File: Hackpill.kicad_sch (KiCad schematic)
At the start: 23 parts, among them J1 Conn_01x04, J2 USB_C_Receptacle_USB2.0_16P, J3 Conn_01x22, J4 Conn_01x22, SW1 SW_Push, U1 STM32F042C6Tx, U2 AMS1117-3.3, U3 USBLC6-2SC6

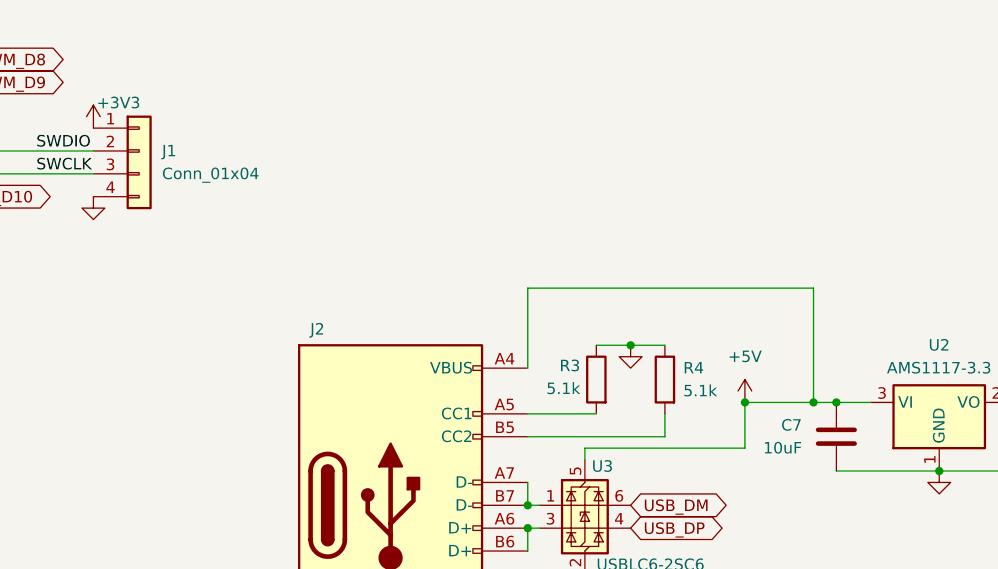
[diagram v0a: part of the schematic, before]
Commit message: Add diode to USB, rename files, add prod files
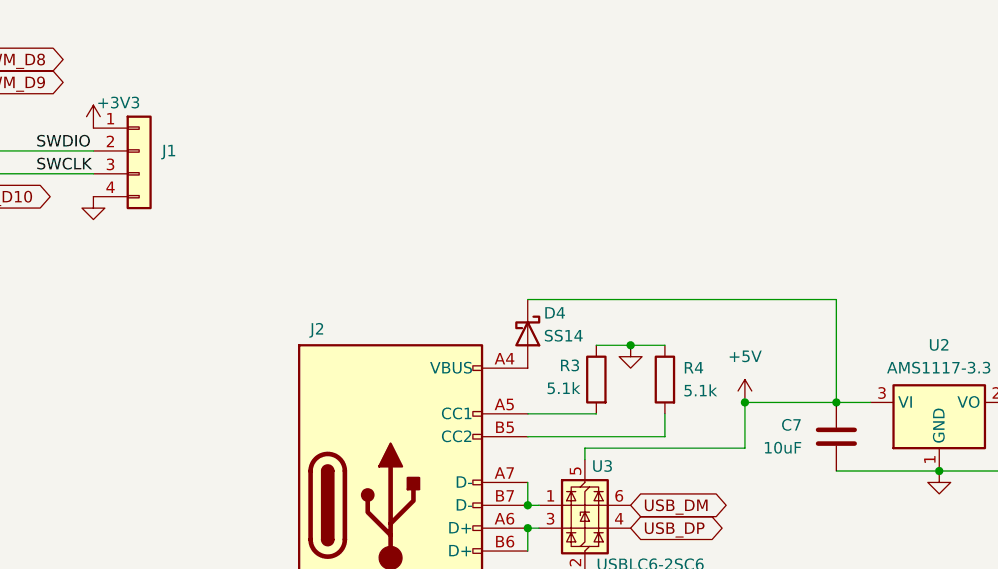
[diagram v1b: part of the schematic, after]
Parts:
- added D4: SS14, Diode_SMD:D_SMA, symbol Diode:SS14
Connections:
- net +5V: now also D4.1 (K); no longer J2.A4 (VBUS), J2.A9 (VBUS), J2.B4 (VBUS), J2.B9 (VBUS)
- new net: D4.2 (A), J2.A4 (VBUS), J2.A9 (VBUS), J2.B4 (VBUS), J2.B9 (VBUS)
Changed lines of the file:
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@@
 	)
 	(junction
-		(at 226.06 104.14)
-		(diameter 0)
-		(color 0 0 0 0)
-	)
-	(junction
 		(at 251.46 104.14)
 		(diameter 0)
@@
 	(wire
 		(pts
-			(xy 226.06 104.14) (xy 228.6 104.14)
+			(xy 171.45 138.43) (xy 179.07 138.43)
 		)
 		(stroke
@@
 	(wire
 		(pts
-			(xy 171.45 138.43) (xy 179.07 138.43)
+			(xy 101.6 29.21) (xy 93.98 29.21)
 		)
 		(stroke
@@
 	(wire
 		(pts
-			(xy 101.6 29.21) (xy 93.98 29.21)
+			(xy 218.44 109.22) (xy 218.44 104.14)
 		)
 		(stroke
@@
 	(wire
 		(pts
-			(xy 218.44 109.22) (xy 218.44 104.14)
+			(xy 121.92 76.2) (xy 146.05 76.2)
 		)
 		(stroke
@@
 	(wire
 		(pts
-			(xy 121.92 76.2) (xy 146.05 76.2)
+			(xy 64.77 43.18) (xy 64.77 44.45)
 		)
 		(stroke
@@
 	(wire
 		(pts
-			(xy 64.77 43.18) (xy 64.77 44.45)
+			(xy 194.31 92.71) (xy 228.6 92.71)
 		)
 		(stroke
@@
 	(wire
 		(pts
-			(xy 218.44 104.14) (xy 226.06 104.14)
+			(xy 218.44 104.14) (xy 228.6 104.14)
 		)
 		(stroke
@@
 	(wire
 		(pts
-			(xy 194.31 100.33) (xy 194.31 91.44)
-		)
-		(stroke
-			(width 0)
-			(type default)
-		)
-	)
-	(wire
-		(pts
 			(xy 71.12 29.21) (xy 59.69 29.21)
 		)
@@
 	(wire
 		(pts
-			(xy 194.31 91.44) (xy 226.06 91.44)
-		)
-		(stroke
-			(width 0)
-			(type default)
-		)
-	)
-	(wire
-		(pts
 			(xy 93.98 29.21) (xy 82.55 29.21)
 		)
@@
 	(wire
 		(pts
-			(xy 226.06 91.44) (xy 226.06 104.14)
+			(xy 228.6 92.71) (xy 228.6 104.14)
 		)
 		(stroke
@@
 		)
 		(instances
-			(project "Workshop_PCB"
+			(project "Hackpill"
 				(path "/c0781056-ba6f-4324-98d3-3fa2d5c57644"
 					(reference "#PWR022")
@@
 		)
 		(instances
-			(project "Workshop_PCB"
+			(project "Hackpill"
 				(path "/c0781056-ba6f-4324-98d3-3fa2d5c57644"
 					(reference "C3")
@@
 		)
 		(instances
-			(project "Workshop_PCB"
+			(project "Hackpill"
 				(path "/c0781056-ba6f-4324-98d3-3fa2d5c57644"
 					(reference "#PWR013")
@@
 		)
 		(instances
-			(project "Workshop_PCB"
+			(project "Hackpill"
 				(path "/c0781056-ba6f-4324-98d3-3fa2d5c57644"
 					(reference "U1")
@@
 		)
 		(instances
-			(project "Workshop_PCB"
+			(project "Hackpill"
 				(path "/c0781056-ba6f-4324-98d3-3fa2d5c57644"
 					(reference "#PWR05")
@@
 		)
 		(instances
-			(project "Workshop_PCB"
+			(project "Hackpill"
 				(path "/c0781056-ba6f-4324-98d3-3fa2d5c57644"
 					(reference "C7")
@@
 		)
 		(instances
-			(project "Workshop_PCB"
+			(project "Hackpill"
 				(path "/c0781056-ba6f-4324-98d3-3fa2d5c57644"
 					(reference "U2")
@@
 		)
 		(instances
-			(project "Workshop_PCB"
+			(project "Hackpill"
 				(path "/c0781056-ba6f-4324-98d3-3fa2d5c57644"
 					(reference "D2")
@@
 		)
 		(instances
-			(project "Workshop_PCB"
+			(project "Hackpill"
 				(path "/c0781056-ba6f-4324-98d3-3fa2d5c57644"
 					(reference "D1")
@@
 		)
 		(instances
-			(project "Workshop_PCB"
+			(project "Hackpill"
 				(path "/c0781056-ba6f-4324-98d3-3fa2d5c57644"
 					(reference "#PWR014")
@@
 		)
 		(instances
-			(project "Workshop_PCB"
+			(project "Hackpill"
 				(path "/c0781056-ba6f-4324-98d3-3fa2d5c57644"
 					(reference "#PWR03")
@@
 		)
 		(instances
-			(project "Workshop_PCB"
+			(project "Hackpill"
 				(path "/c0781056-ba6f-4324-98d3-3fa2d5c57644"
 					(reference "#PWR024")
@@
 		)
 		(instances
-			(project "Workshop_PCB"
+			(project "Hackpill"
 				(path "/c0781056-ba6f-4324-98d3-3fa2d5c57644"
 					(reference "C8")
@@
 		)
 		(instances
-			(project "Workshop_PCB"
+			(project "Hackpill"
 				(path "/c0781056-ba6f-4324-98d3-3fa2d5c57644"
 					(reference "#PWR015")
@@
 		)
 		(instances
-			(project "Workshop_PCB"
+			(project "Hackpill"
 				(path "/c0781056-ba6f-4324-98d3-3fa2d5c57644"
 					(reference "R4")
@@
 		)
 		(instances
-			(project "Workshop_PCB"
+			(project "Hackpill"
 				(path "/c0781056-ba6f-4324-98d3-3fa2d5c57644"
 					(reference "C6")
@@
 		)
 		(instances
-			(project "Workshop_PCB"
+			(project "Hackpill"
 				(path "/c0781056-ba6f-4324-98d3-3fa2d5c57644"
 					(reference "C5")
@@
 		)
 		(instances
-			(project "Workshop_PCB"
+			(project "Hackpill"
 				(path "/c0781056-ba6f-4324-98d3-3fa2d5c57644"
 					(reference "J2")
@@
 		)
 		(instances
-			(project "Workshop_PCB"
+			(project "Hackpill"
 				(path "/c0781056-ba6f-4324-98d3-3fa2d5c57644"
 					(reference "SW1")
@@
 		)
 		(instances
-			(project "Workshop_PCB"
+			(project "Hackpill"
 				(path "/c0781056-ba6f-4324-98d3-3fa2d5c57644"
 					(reference "#PWR021")
@@
 		)
 		(instances
-			(project "Workshop_PCB"
+			(project "Hackpill"
 				(path "/c0781056-ba6f-4324-98d3-3fa2d5c57644"
 					(reference "#PWR020")
@@
 		)
 		(instances
-			(project "Workshop_PCB"
+			(project "Hackpill"
 				(path "/c0781056-ba6f-4324-98d3-3fa2d5c57644"
 					(reference "#PWR06")
@@
 				)
 				(justify left)
+				(hide yes)
 			)
 		)
@@
 		)
 		(instances
-			(project "Workshop_PCB"
+			(project "Hackpill"
 				(path "/c0781056-ba6f-4324-98d3-3fa2d5c57644"
 					(reference "J1")
@@
 		)
 		(instances
-			(project "Workshop_PCB"
+			(project "Hackpill"
 				(path "/c0781056-ba6f-4324-98d3-3fa2d5c57644"
 					(reference "U3")
@@
 		)
 		(instances
-			(project "Workshop_PCB"
+			(project "Hackpill"
 				(path "/c0781056-ba6f-4324-98d3-3fa2d5c57644"
 					(reference "#PWR08")
@@
 		)
 		(instances
-			(project "Workshop_PCB"
+			(project "Hackpill"
 				(path "/c0781056-ba6f-4324-98d3-3fa2d5c57644"
 					(reference "#PWR02")
@@
 		)
 		(instances
-			(project "Workshop_PCB"
+			(project "Hackpill"
 				(path "/c0781056-ba6f-4324-98d3-3fa2d5c57644"
 					(reference "C2")
@@
 		)
 		(instances
-			(project "Workshop_PCB"
+			(project "Hackpill"
 				(path "/c0781056-ba6f-4324-98d3-3fa2d5c57644"
 					(reference "#PWR09")
@@
 		)
 		(instances
-			(project "Workshop_PCB"
+			(project "Hackpill"
 				(path "/c0781056-ba6f-4324-98d3-3fa2d5c57644"
 					(reference "#PWR018")
@@
 		)
 		(instances
-			(project "Workshop_PCB"
+			(project "Hackpill"
 				(path "/c0781056-ba6f-4324-98d3-3fa2d5c57644"
 					(reference "#PWR011")
@@
 		)
 		(instances
-			(project "Workshop_PCB"
+			(project "Hackpill"
 				(path "/c0781056-ba6f-4324-98d3-3fa2d5c57644"
 					(reference "C4")
@@
 		)
 		(instances
-			(project "Workshop_PCB"
+			(project "Hackpill"
 				(path "/c0781056-ba6f-4324-98d3-3fa2d5c57644"
 					(reference "R1")
@@
 		)
 		(instances
-			(project "Workshop_PCB"
+			(project "Hackpill"
 				(path "/c0781056-ba6f-4324-98d3-3fa2d5c57644"
 					(reference "J4")
@@
 		)
 		(instances
-			(project "Workshop_PCB"
+			(project "Hackpill"
 				(path "/c0781056-ba6f-4324-98d3-3fa2d5c57644"
 					(reference "#PWR01")
@@
 		)
 		(instances
-			(project "Workshop_PCB"
+			(project "Hackpill"
 				(path "/c0781056-ba6f-4324-98d3-3fa2d5c57644"
 					(reference "R5")
@@
 		)
 		(instances
-			(project "Workshop_PCB"
+			(project "Hackpill"
 				(path "/c0781056-ba6f-4324-98d3-3fa2d5c57644"
 					(reference "#PWR07")
@@
 	)
 	(symbol
+		(lib_id "Diode:SS14")
+		(at 194.31 96.52 270)
+		(unit 1)
+		(exclude_from_sim no)
+		(in_bom yes)
+		(on_board yes)
+		(dnp no)
+		(property "Reference" "D4"
+			(at 196.088 94.234 90)
+			(effects
+				(font
+					(size 1.27 1.27)
+				)
+				(justify left)
+			)
+		)
+		(property "Value" "SS14"
+			(at 196.088 96.774 90)
+			(effects
+				(font
+					(size 1.27 1.27)
+				)
+				(justify left)
+			)
+		)
+		(property "Footprint" "Diode_SMD:D_SMA"
+			(at 189.865 96.52 0)
+			(effects
+				(font
+					(size 1.27 1.27)
+				)
+				(hide yes)
+			)
+		)
+		(property "Datasheet" "https://www.vishay.com/docs/88746/ss12.pdf"
+			(at 194.31 96.52 0)
+			(effects
+				(font
+					(size 1.27 1.27)
+				)
+				(hide yes)
+			)
+		)
+		(property "Description" "40V 1A Schottky Diode, SMA"
+			(at 194.31 96.52 0)
+			(effects
+				(font
+					(size 1.27 1.27)
+				)
+				(hide yes)
+			)
+		)
+		(pin "1"
+		)
+		(pin "2"
+		)
+		(instances
+			(project "Hackpill"
+				(path "/c0781056-ba6f-4324-98d3-3fa2d5c57644"
+					(reference "D4")
+					(unit 1)
+				)
+			)
+		)
+	)
+	(symbol
 		(lib_id "Device:R")
 		(at 201.93 101.6 0)
@@
 		)
 		(instances
-			(project "Workshop_PCB"
+			(project "Hackpill"
 				(path "/c0781056-ba6f-4324-98d3-3fa2d5c57644"
 					(reference "R3")
@@
 		)
 		(instances
-			(project "Workshop_PCB"
+			(project "Hackpill"
 				(path "/c0781056-ba6f-4324-98d3-3fa2d5c57644"
 					(reference "#PWR019")
@@
 		)
 		(instances
-			(project "Workshop_PCB"
+			(project "Hackpill"
 				(path "/c0781056-ba6f-4324-98d3-3fa2d5c57644"
 					(reference "#PWR04")
@@
 		)
 		(instances
-			(project "Workshop_PCB"
+			(project "Hackpill"
 				(path "/c0781056-ba6f-4324-98d3-3fa2d5c57644"
 					(reference "J3")
@@
 		)
 		(instances
-			(project "Workshop_PCB"
+			(project "Hackpill"
 				(path "/c0781056-ba6f-4324-98d3-3fa2d5c57644"
 					(reference "R2")
@@
 		)
 		(instances
-			(project "Workshop_PCB"
+			(project "Hackpill"
 				(path "/c0781056-ba6f-4324-98d3-3fa2d5c57644"
 					(reference "C1")
@@
 		)
 		(instances
-			(project "Workshop_PCB"
+			(project "Hackpill"
 				(path "/c0781056-ba6f-4324-98d3-3fa2d5c57644"
 					(reference "#PWR010")

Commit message: Change clearence, update footprint, add README, add schematic, remove config file
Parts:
- J1: LCSC (none) -> C18905864
- J2: footprint Connector_USB:USB_C_Receptacle_Hanbo_16P_TopMnt_Horizontal -> Connector_USB:USB_C_Receptacle_Shouhan_16P_TopMnt_Horizontal
- J4: LCSC (none) -> C18078140
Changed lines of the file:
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@@
 			)
 		)
-		(property "Footprint" "Connector_USB:USB_C_Receptacle_Hanbo_16P_TopMnt_Horizontal"
+		(property "Footprint" "Connector_USB:USB_C_Receptacle_Shouhan_16P_TopMnt_Horizontal"
 			(at 182.88 115.57 0)
 			(effects
@@
 			)
 		)
-		(property "LCSC" ""
+		(property "LCSC" "C18905864"
 			(at 151.13 76.2 0)
 			(effects
@@
 			)
 		)
-		(property "LCSC" ""
+		(property "LCSC" "C18078140"
 			(at 69.85 151.13 0)
 			(effects
